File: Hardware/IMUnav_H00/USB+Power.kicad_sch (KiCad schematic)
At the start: 67 parts, among them J1 918-418K2023S40001, Q3 2N7002, SW1 MT-102, SW2 SW_DPST, U1 USB2514B-AEZC-TR, U14 HT7533-1, U16 74LVC2G02, U17 BQ24075RGT, U4 TPS62823DLC, U5 USBLC6-2P6, U6 TVS0500DRV, X1 SX5M24.000M20F30TNN

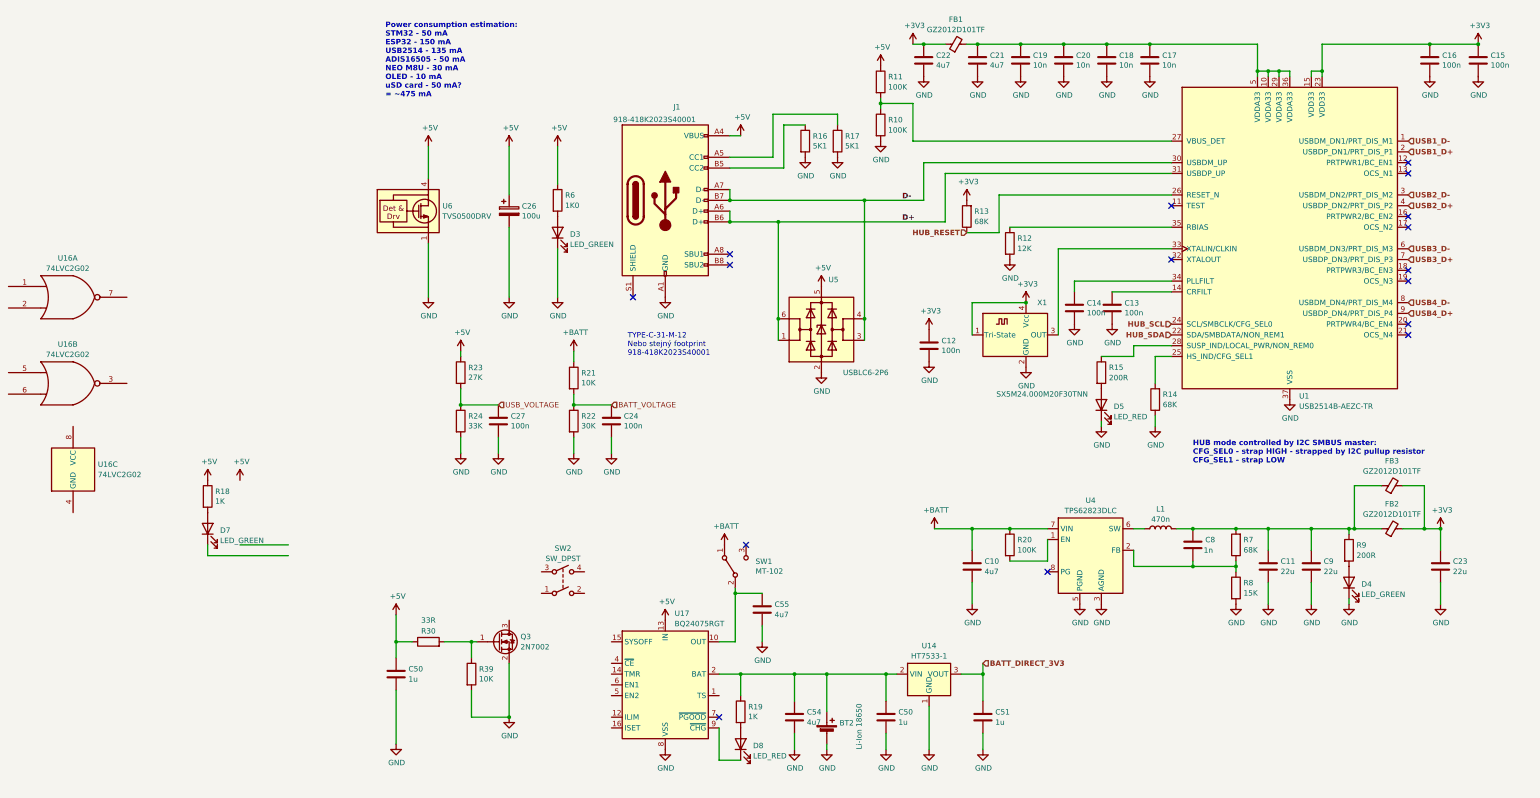
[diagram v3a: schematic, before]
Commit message: Finalized and cleaned Power Management, added GPS antenna footprint
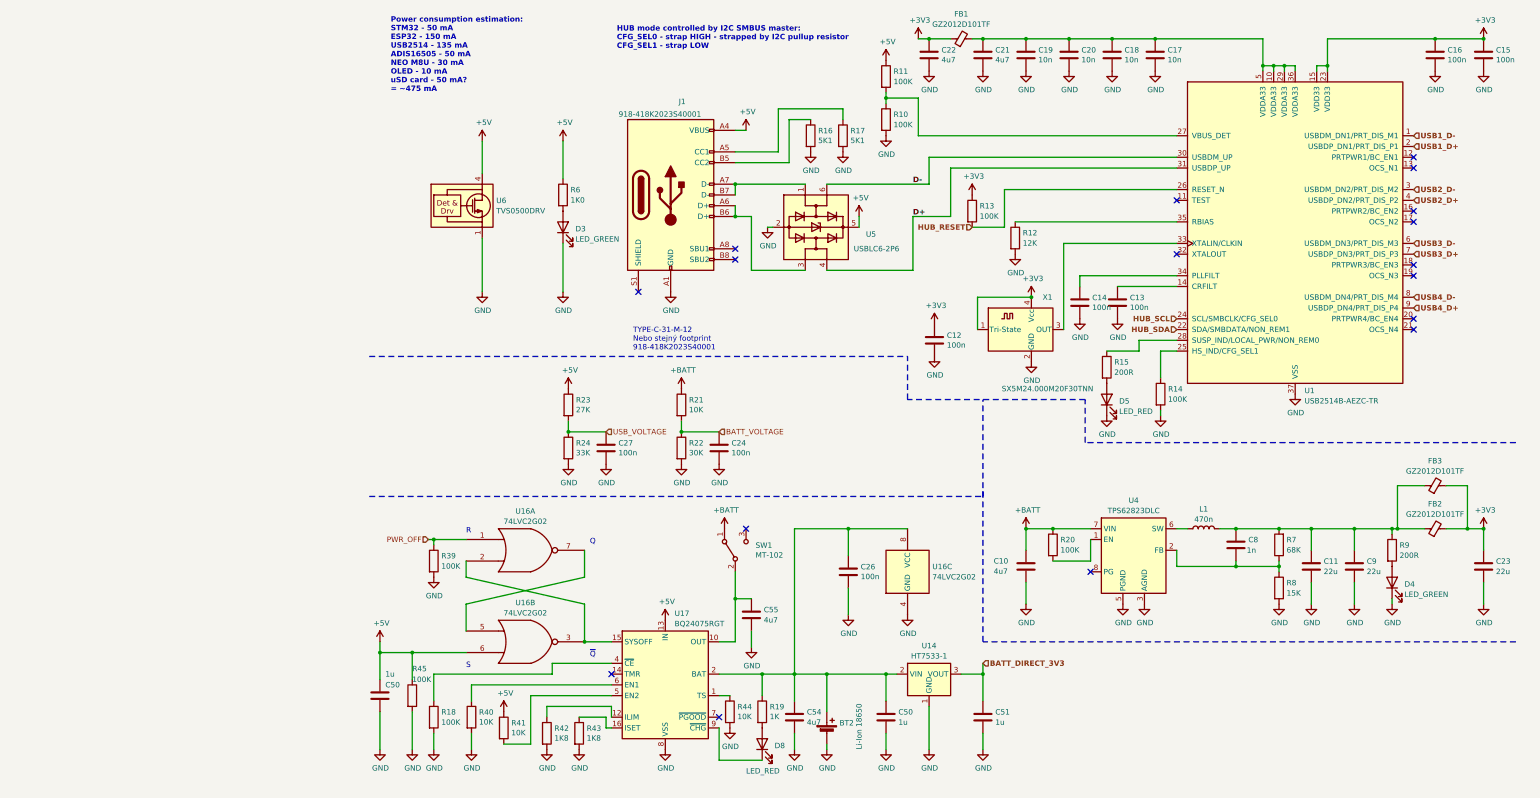
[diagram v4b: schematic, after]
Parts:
- removed C26: 100u, Capacitor_THT:CP_Radial_D5.0mm_P2.00mm, symbol Device:C_Polarized
- removed D7: LED_GREEN, LED_SMD:LED_0603_1608Metric, symbol Device:LED
- removed Q3: 2N7002, Package_TO_SOT_SMD:SOT-23, symbol Transistor_FET:2N7002
- removed R30: 33R, Resistor_SMD:R_0603_1608Metric, symbol Device:R
- removed SW2: SW_DPST, symbol Switch:SW_DPST
- added C26: 100n, Capacitor_SMD:C_0603_1608Metric, symbol Device:C
- added R40, R41, R44: 10K, Resistor_SMD:R_0603_1608Metric, symbol Device:R
- added R42, R43: 1K8, Resistor_SMD:R_0603_1608Metric, symbol Device:R
- added R45: 100K, Resistor_SMD:R_0603_1608Metric, symbol Device:R
- R13, R14: value 68K -> 100K; LCSC C23231 -> C25803
- R18: value 1K -> 100K; LCSC C21190 -> C25803
- R39: value 10K -> 100K; LCSC C25804 -> C25803
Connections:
- net +3V3: now also R13.1; no longer R13.2
- net +5V: now also U16.6, R41.1, R45.1; no longer R18.1
- net D+: now also U5.4 (I/O2); no longer J1.A6 (D+), J1.B6 (D+), U5.1 (I/O1), U5.6 (I/O1)
- net D-: now also U5.6 (I/O1); no longer J1.A7 (D-), J1.B7 (D-), U5.3 (I/O2), U5.4 (I/O2)
- net GND: now also R14.2, R18.2, U16.4 (GND), C26.2, R40.2, R42.2, R43.2, R44.2, R45.2; no longer R14.1
- net HUB_RESET: now also R13.2; no longer R13.1
- net at U1.25 (HS_IND/CFG_SEL1): now also R14.1; no longer R14.2
- net at U17.1 (TS): now also R44.1
- net at U17.12 (ILIM): now also R42.1
- net at U17.15 (SYSOFF): now also U16.2, U16.3
- net at U17.16 (ISET): now also R43.1
- net at BT2.1 (+), C50.1, C54.1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: now also U16.8 (VCC), C26.1
- net at U17.4 (~{CE}): now also R18.1
- net at U17.5 (EN2): now also R41.2
- net at U17.6 (EN1): now also R40.1
- net PWR_OFF: now reaches R39.1
- net PWR_OFF: now also U16.1
- net at U16.7: now also U16.5
- new net: J1.A6 (D+), J1.B6 (D+), U5.3 (I/O2)
- new net: J1.A7 (D-), J1.B7 (D-), U5.1 (I/O1)
- no-connect marks 16 -> 17
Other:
- note added: "Q"
- note added: "R"
- note added: "S"
- note added: "~{Q}"
- moved on the sheet: C10, C11, C12, C13, C14, C15, C16, C17, C18, C19, C20, C21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

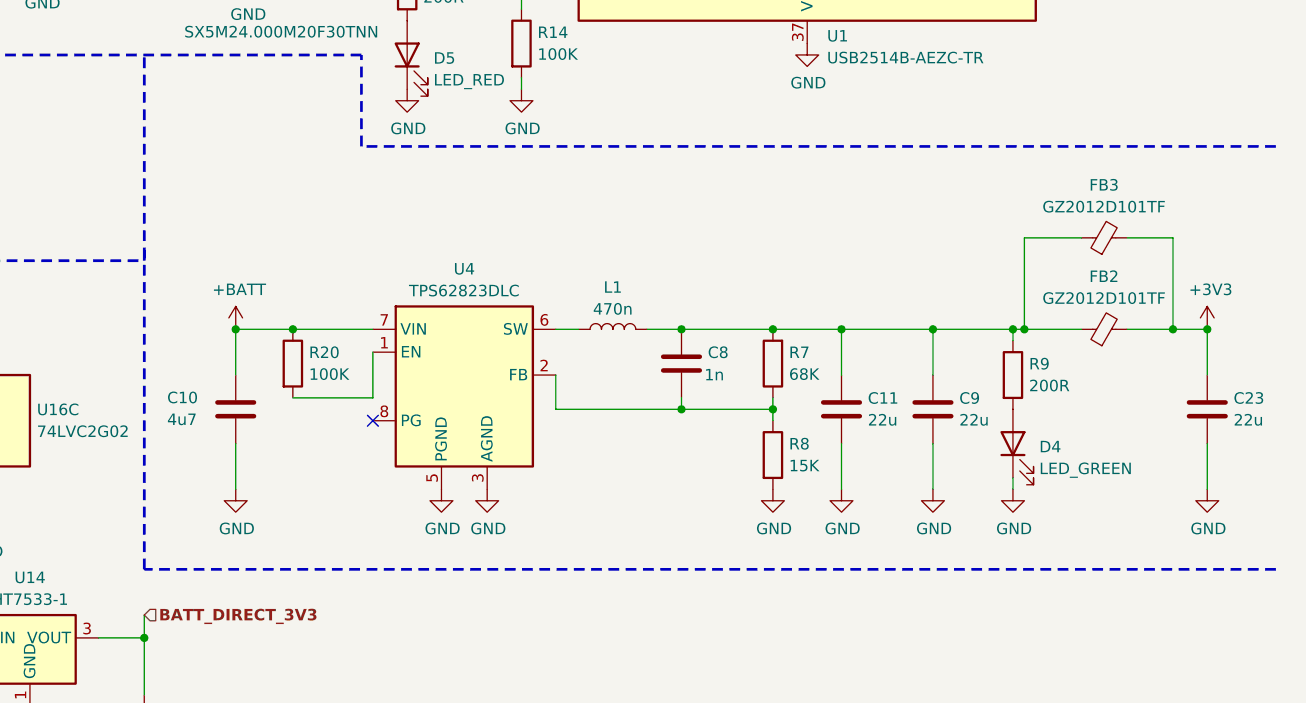
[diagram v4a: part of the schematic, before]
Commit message: Added sheets for memory and UserInterface
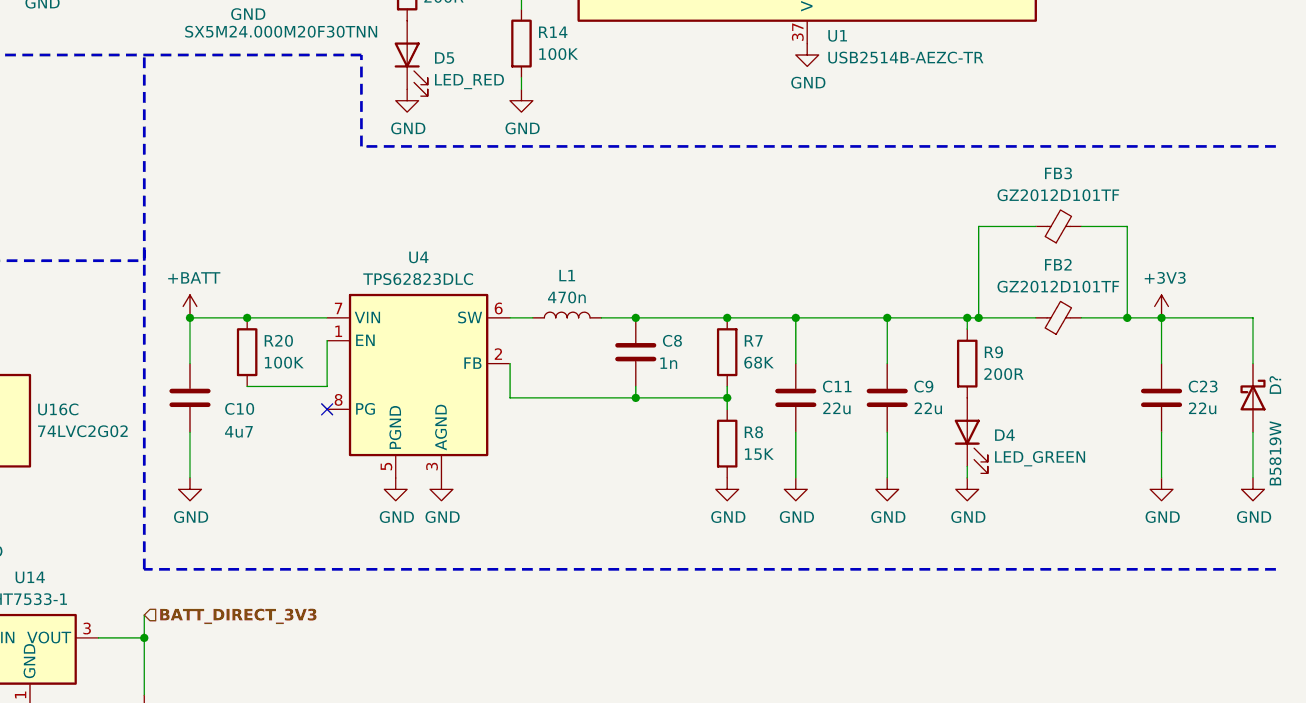
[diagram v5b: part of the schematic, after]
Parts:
- added D?: B5819W, Diode_SMD:D_SOD-123, symbol Device:D_Schottky
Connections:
- net +3V3: now also D?.1 (K)
- net GND: now also D?.2 (A)
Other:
- moved on the sheet: C10, C11, C23, C8, C9, D4, FB2, FB3, L1, R20, R7, R8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

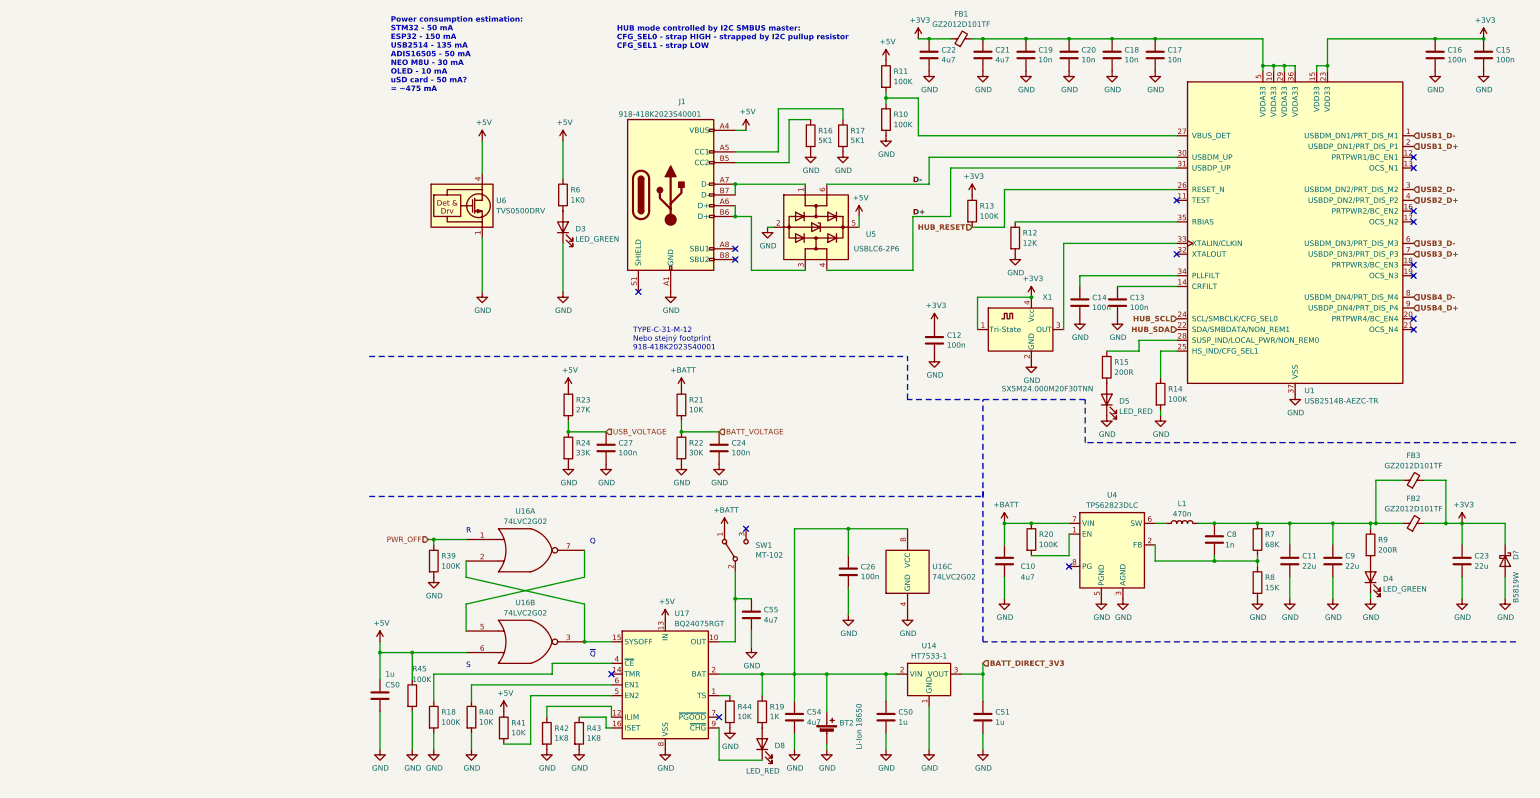
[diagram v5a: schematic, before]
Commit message: Added signal connections to MCU+misc
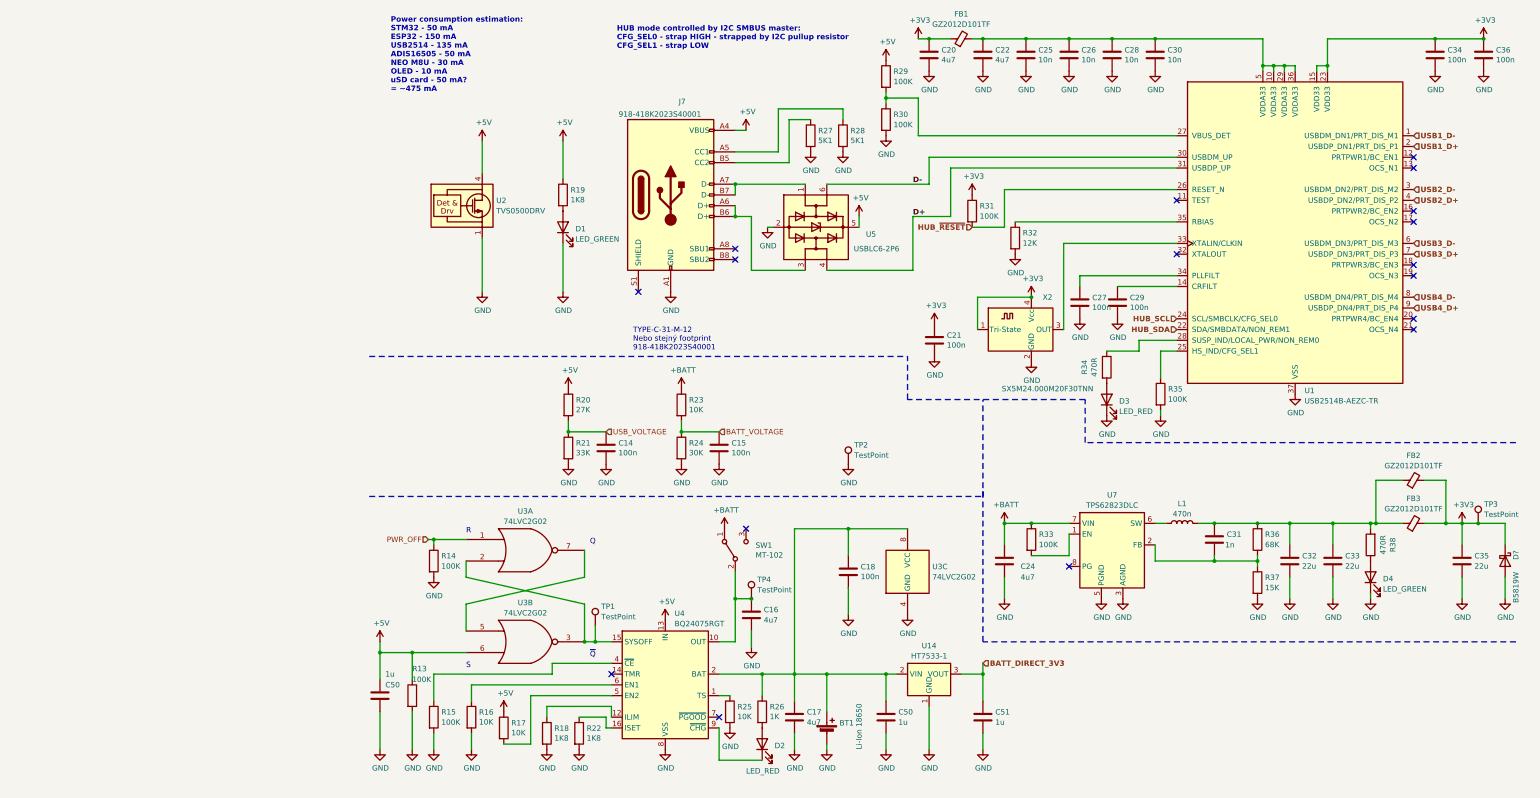
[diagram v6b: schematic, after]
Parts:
- removed R15, R9: 200R, Resistor_SMD:R_0603_1608Metric, symbol Device:R
- removed R6: 1K0, Resistor_SMD:R_0603_1608Metric, symbol Device:R
- added R19: 1K8, Resistor_SMD:R_0603_1608Metric, symbol Device:R
- added R34, R38: 470R, Resistor_SMD:R_0603_1608Metric, symbol Device:R
- added TP1, TP2, TP3, TP4: TestPoint, TestPoint:TestPoint_Keystone_5005-5009_Compact, symbol Connector:TestPoint
- U3: renamed from U16; footprint (none) -> Package_SO:VSSOP-8_2.3x2mm_P0.5mm
- renumbered BT2 to BT1, C27 to C14, C24 to C15, C55 to C16, C54 to C17, C26 to C18, C22 to C20, C12 to C21, C21 to C22, C10 to C24, C19 to C25, C20 to C26, C14 to C27, C18 to C28, C13 to C29, C17 to C30, C8 to C31, C11 to C32, C9 to C33, C16 to C34, C23 to C35, C15 to C36, D3 to D1, D8 to D2, D5 to D3, FB3 to FB2, FB2 to FB3, J1 to J7, R45 to R13, R39 to R14, R18 to R15, R40 to R16, R41 to R17, R42 to R18, R23 to R20, R24 to R21, R43 to R22, R21 to R23, R22 to R24, R44 to R25, R19 to R26, R16 to R27, R17 to R28, R11 to R29, R10 to R30, R13 to R31, R12 to R32, R20 to R33, R14 to R35, R7 to R36, R8 to R37, U6 to U2, U17 to U4, U4 to U7, X1 to X2
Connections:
- net +3V3: now also TP3.1
- net +5V: now also R19.1
- net GND: now also TP2.1
- net at C16.1, SW1.2 (B), U4.10 (OUT)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: now also TP4.1
- net at C31.1, C32.1, C33.1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: now also R38.2
- net at U1.28 (SUSP_IND/LOCAL_PWR/NON_REM0): now also R34.1
- net at U3.2, U3.3, U4.15 (SYSOFF): now also TP1.1
- net at D1.2 (A): now also R19.2
- net at D3.2 (A): now also R34.2
- net at D4.2 (A): now also R38.1
- net HUB_RESET renamed HUB_~{RESET}

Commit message: Changed LSM303C to LSM303AGR
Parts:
- U2: LCSC (none) -> C609571
- U4: LCSC (none) -> C15464
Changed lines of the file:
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@@
+      (effects (font (size 1.27 1.27)) hide)
+    )
+    (property "LCSC" "C15464" (at 82.55 172.72 0)
       (effects (font (size 1.27 1.27)) hide)
     )
@@
       (effects (font (size 1.27 1.27)) hide)
     )
+    (property "LCSC" "C609571" (at 39.37 59.69 0)
+      (effects (font (size 1.27 1.27)) hide)
+    )

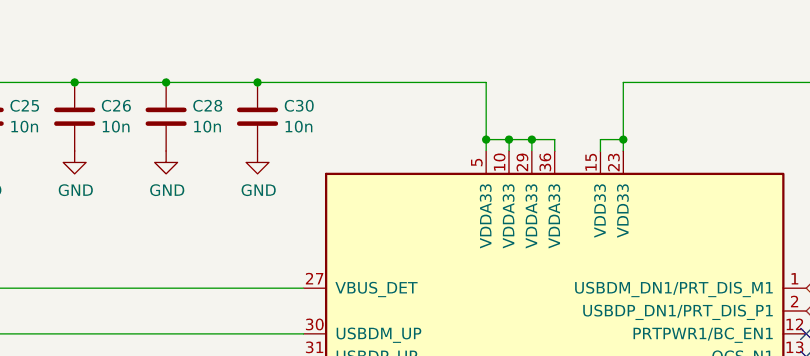
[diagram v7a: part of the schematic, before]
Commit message: PCB layout - BGA fanout, GPS and USB hub
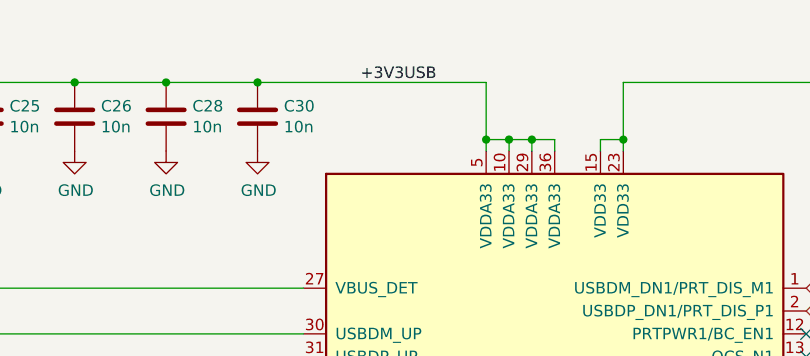
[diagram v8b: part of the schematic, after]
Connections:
- net +3V3USB: now reaches C22.1, C25.1, C26.1, C28.1, C30.1, FB1.2, U1.10 (VDDA33), U1.29 (VDDA33), U1.36 (VDDA33), U1.5 (VDDA33)
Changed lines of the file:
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@@
+    (effects (font (size 1.27 1.27)) (justify left bottom))
+  )
+  (label "+3V3USB" (at 209.55 20.32 0) (fields_autoplaced)
     (effects (font (size 1.27 1.27)) (justify left bottom))
   )
